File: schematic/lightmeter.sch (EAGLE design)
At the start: 67 parts, among them Q1 NCHANNELMOSFET, Q2 NCHANNELMOSFET, Q3 PCHANNELMOSFET

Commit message: More work on pcb layout.
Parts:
- renumbered R100 to R2, R1300 to R13, R1400 to R14, R200 to R1, R600 to R6, R800 to R8
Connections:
- removed net N$2: D2.A
- net VUSB: now also D2.A
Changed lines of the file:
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@@
 <part name="R700" library="resistor" deviceset="R-EU_" device="R0402" value="10k"/>
 <part name="GND8" library="supply1" deviceset="GND" device=""/>
-<part name="R800" library="resistor" deviceset="R-EU_" device="R0402" value="390k"/>
+<part name="R8" library="resistor" deviceset="R-EU_" device="R0402" value="390k"/>
 <part name="C15" library="rcl" deviceset="C-EU" device="C0402" value="1u"/>
 <part name="C16" library="rcl" deviceset="C-EU" device="C0402" value="1u"/>
@@
 <part name="GND28" library="supply1" deviceset="GND" device=""/>
 <part name="GND31" library="supply1" deviceset="GND" device=""/>
-<part name="R100" library="resistor" deviceset="R-EU_" device="R0402" value="15k"/>
-<part name="R200" library="resistor" deviceset="R-EU_" device="R0402" value="15k"/>
+<part name="R2" library="resistor" deviceset="R-EU_" device="R0402" value="15k"/>
+<part name="R1" library="resistor" deviceset="R-EU_" device="R0402" value="15k"/>
 <part name="GND9" library="supply1" deviceset="GND" device=""/>
 <part name="GND33" library="supply1" deviceset="GND" device=""/>
@@
 <part name="C24" library="rcl" deviceset="C-EU" device="C0402" value="1u"/>
 <part name="U$3" library="lightmeter" deviceset="LIBAT" device=""/>
-<part name="R1300" library="resistor" deviceset="R-EU_" device="R0402" value="500k"/>
-<part name="R1400" library="resistor" deviceset="R-EU_" device="R0402" value="500k"/>
+<part name="R13" library="resistor" deviceset="R-EU_" device="R0402" value="500k"/>
+<part name="R14" library="resistor" deviceset="R-EU_" device="R0402" value="500k"/>
 <part name="GND7" library="supply1" deviceset="GND" device=""/>
 <part name="P+4" library="supply1" deviceset="VCC" device=""/>
@@
 <part name="D3" library="lightmeter" deviceset="GSOT04-E3-08" device=""/>
 <part name="GND32" library="supply1" deviceset="GND" device=""/>
-<part name="R600" library="resistor" deviceset="R-EU_" device="R0402" value="10k"/>
+<part name="R6" library="resistor" deviceset="R-EU_" device="R0402" value="10k"/>
 <part name="IC$7" library="lightmeter" deviceset="NOA1212" device=""/>
 <part name="IC$8" library="lightmeter" deviceset="NOA1212" device=""/>
@@
 <instance part="R700" gate="G$1" x="160.02" y="0"/>
 <instance part="GND8" gate="1" x="-55.118" y="-108.458" rot="R270"/>
-<instance part="R800" gate="G$1" x="177.8" y="-10.16"/>
+<instance part="R8" gate="G$1" x="177.8" y="-10.16"/>
 <instance part="C15" gate="G$1" x="193.04" y="50.8" rot="R90"/>
 <instance part="C16" gate="G$1" x="177.8" y="48.26" rot="R90"/>
@@
 <instance part="GND28" gate="1" x="11.684" y="-118.618" rot="R90"/>
 <instance part="GND31" gate="1" x="-99.06" y="93.98" rot="R270"/>
-<instance part="R100" gate="G$1" x="-111.76" y="88.9"/>
-<instance part="R200" gate="G$1" x="-113.538" y="86.36"/>
+<instance part="R2" gate="G$1" x="-111.76" y="88.9"/>
+<instance part="R1" gate="G$1" x="-113.538" y="86.36"/>
 <instance part="GND9" gate="1" x="-117.856" y="98.298" rot="R180"/>
 <instance part="GND33" gate="1" x="-118.618" y="78.74"/>
@@
 <instance part="C24" gate="G$1" x="-76.2" y="-78.74"/>
 <instance part="U$3" gate="G$1" x="-132.08" y="-12.7"/>
-<instance part="R1300" gate="G$1" x="-111.76" y="-124.46"/>
-<instance part="R1400" gate="G$1" x="-91.44" y="-124.46"/>
+<instance part="R13" gate="G$1" x="-111.76" y="-124.46"/>
+<instance part="R14" gate="G$1" x="-91.44" y="-124.46"/>
 <instance part="GND7" gate="1" x="-81.788" y="-124.46" rot="R90"/>
 <instance part="P+4" gate="VCC" x="-124.46" y="-124.46" rot="R90"/>
@@
 <instance part="D3" gate="G$1" x="96.52" y="40.64" rot="R90"/>
 <instance part="GND32" gate="1" x="96.52" y="20.32"/>
-<instance part="R600" gate="G$1" x="96.52" y="30.48" rot="R90"/>
+<instance part="R6" gate="G$1" x="96.52" y="30.48" rot="R90"/>
 <instance part="IC$7" gate="G$1" x="167.64" y="-60.96"/>
 <instance part="IC$8" gate="G$1" x="167.64" y="-86.36"/>
@@
 <wire x1="152.4" y1="-17.78" x2="152.4" y2="-20.32" width="0.1524" layer="91"/>
 <pinref part="GND15" gate="1" pin="GND"/>
-<pinref part="R800" gate="G$1" pin="1"/>
+<pinref part="R8" gate="G$1" pin="1"/>
 <wire x1="172.72" y1="-10.16" x2="152.4" y2="-10.16" width="0.1524" layer="91"/>
 <wire x1="152.4" y1="-10.16" x2="152.4" y2="-17.78" width="0.1524" layer="91"/>
@@
 <wire x1="-118.618" y1="81.28" x2="-118.618" y2="86.36" width="0.1524" layer="91"/>
 <pinref part="GND33" gate="1" pin="GND"/>
-<pinref part="R200" gate="G$1" pin="1"/>
+<pinref part="R1" gate="G$1" pin="1"/>
 </segment>
 <segment>
@@
 <wire x1="-117.856" y1="88.9" x2="-117.856" y2="95.758" width="0.1524" layer="91"/>
 <pinref part="GND9" gate="1" pin="GND"/>
-<pinref part="R100" gate="G$1" pin="1"/>
+<pinref part="R2" gate="G$1" pin="1"/>
 </segment>
 <segment>
@@
 </segment>
 <segment>
-<pinref part="R1400" gate="G$1" pin="2"/>
+<pinref part="R14" gate="G$1" pin="2"/>
 <wire x1="-86.36" y1="-124.46" x2="-84.328" y2="-124.46" width="0.1524" layer="91"/>
 <pinref part="GND7" gate="1" pin="GND"/>
 </segment>
 <segment>
-<pinref part="R600" gate="G$1" pin="1"/>
+<pinref part="R6" gate="G$1" pin="1"/>
 <pinref part="GND32" gate="1" pin="GND"/>
 <wire x1="96.52" y1="25.4" x2="96.52" y2="22.86" width="0.1524" layer="91"/>
@@
 </segment>
 <segment>
-<pinref part="R1300" gate="G$1" pin="1"/>
+<pinref part="R13" gate="G$1" pin="1"/>
 <pinref part="P+4" gate="VCC" pin="VCC"/>
 <wire x1="-121.92" y1="-124.46" x2="-116.84" y2="-124.46" width="0.1524" layer="91"/>
@@
 <pinref part="IC$4" gate="G$1" pin="IREF"/>
 <wire x1="203.2" y1="-10.16" x2="182.88" y2="-10.16" width="0.1524" layer="91"/>
-<pinref part="R800" gate="G$1" pin="2"/>
+<pinref part="R8" gate="G$1" pin="2"/>
 </segment>
 </net>
@@
 <pinref part="U1" gate="G$1" pin="VBUS"/>
 <wire x1="-88.9" y1="83.82" x2="-96.52" y2="83.82" width="0.1524" layer="91"/>
+</segment>
+<segment>
+<wire x1="-137.16" y1="-48.26" x2="-139.7" y2="-48.26" width="0.1524" layer="91"/>
+<wire x1="-137.16" y1="-48.26" x2="-137.16" y2="-38.1" width="0.1524" layer="91"/>
+<pinref part="D2" gate="G$1" pin="A"/>
+<wire x1="-132.08" y1="-38.1" x2="-137.16" y2="-38.1" width="0.1524" layer="91"/>
+<label x="-139.7" y="-48.26" size="1.778" layer="95" rot="R180" xref="yes"/>
 </segment>
 </net>
@@
 <segment>
 <wire x1="-88.9" y1="88.9" x2="-101.6" y2="88.9" width="0.1524" layer="91"/>
-<pinref part="R100" gate="G$1" pin="2"/>
+<pinref part="R2" gate="G$1" pin="2"/>
 <pinref part="U1" gate="G$1" pin="D+"/>
 <wire x1="-101.6" y1="88.9" x2="-106.68" y2="88.9" width="0.1524" layer="91"/>
@@
 <net name="BATVOLTAGE" class="0">
 <segment>
-<pinref part="R1300" gate="G$1" pin="2"/>
-<pinref part="R1400" gate="G$1" pin="1"/>
+<pinref part="R13" gate="G$1" pin="2"/>
+<pinref part="R14" gate="G$1" pin="1"/>
 <wire x1="-106.68" y1="-124.46" x2="-96.52" y2="-124.46" width="0.1524" layer="91"/>
 <label x="-101.6" y="-124.46" size="1.778" layer="95" rot="R90" xref="yes"/>
@@
 <net name="N$13" class="0">
 <segment>
-<pinref part="R600" gate="G$1" pin="2"/>
+<pinref part="R6" gate="G$1" pin="2"/>
 <pinref part="D3" gate="G$1" pin="A"/>
 <wire x1="96.52" y1="35.56" x2="96.52" y2="38.1" width="0.1524" layer="91"/>
@@
 <segment>
 <wire x1="-88.9" y1="86.36" x2="-99.06" y2="86.36" width="0.1524" layer="91"/>
-<pinref part="R200" gate="G$1" pin="2"/>
+<pinref part="R1" gate="G$1" pin="2"/>
 <pinref part="U1" gate="G$1" pin="D-"/>
 <wire x1="-99.06" y1="86.36" x2="-108.458" y2="86.36" width="0.1524" layer="91"/>
@@
 </segment>
 </net>
-<net name="N$2" class="0">
-<segment>
-<wire x1="-137.16" y1="-48.26" x2="-139.7" y2="-48.26" width="0.1524" layer="91"/>
-<wire x1="-137.16" y1="-48.26" x2="-137.16" y2="-38.1" width="0.1524" layer="91"/>
-<pinref part="D2" gate="G$1" pin="A"/>
-<wire x1="-132.08" y1="-38.1" x2="-137.16" y2="-38.1" width="0.1524" layer="91"/>
-<label x="-139.7" y="-48.26" size="1.778" layer="95" rot="R180" xref="yes"/>
-</segment>
-</net>

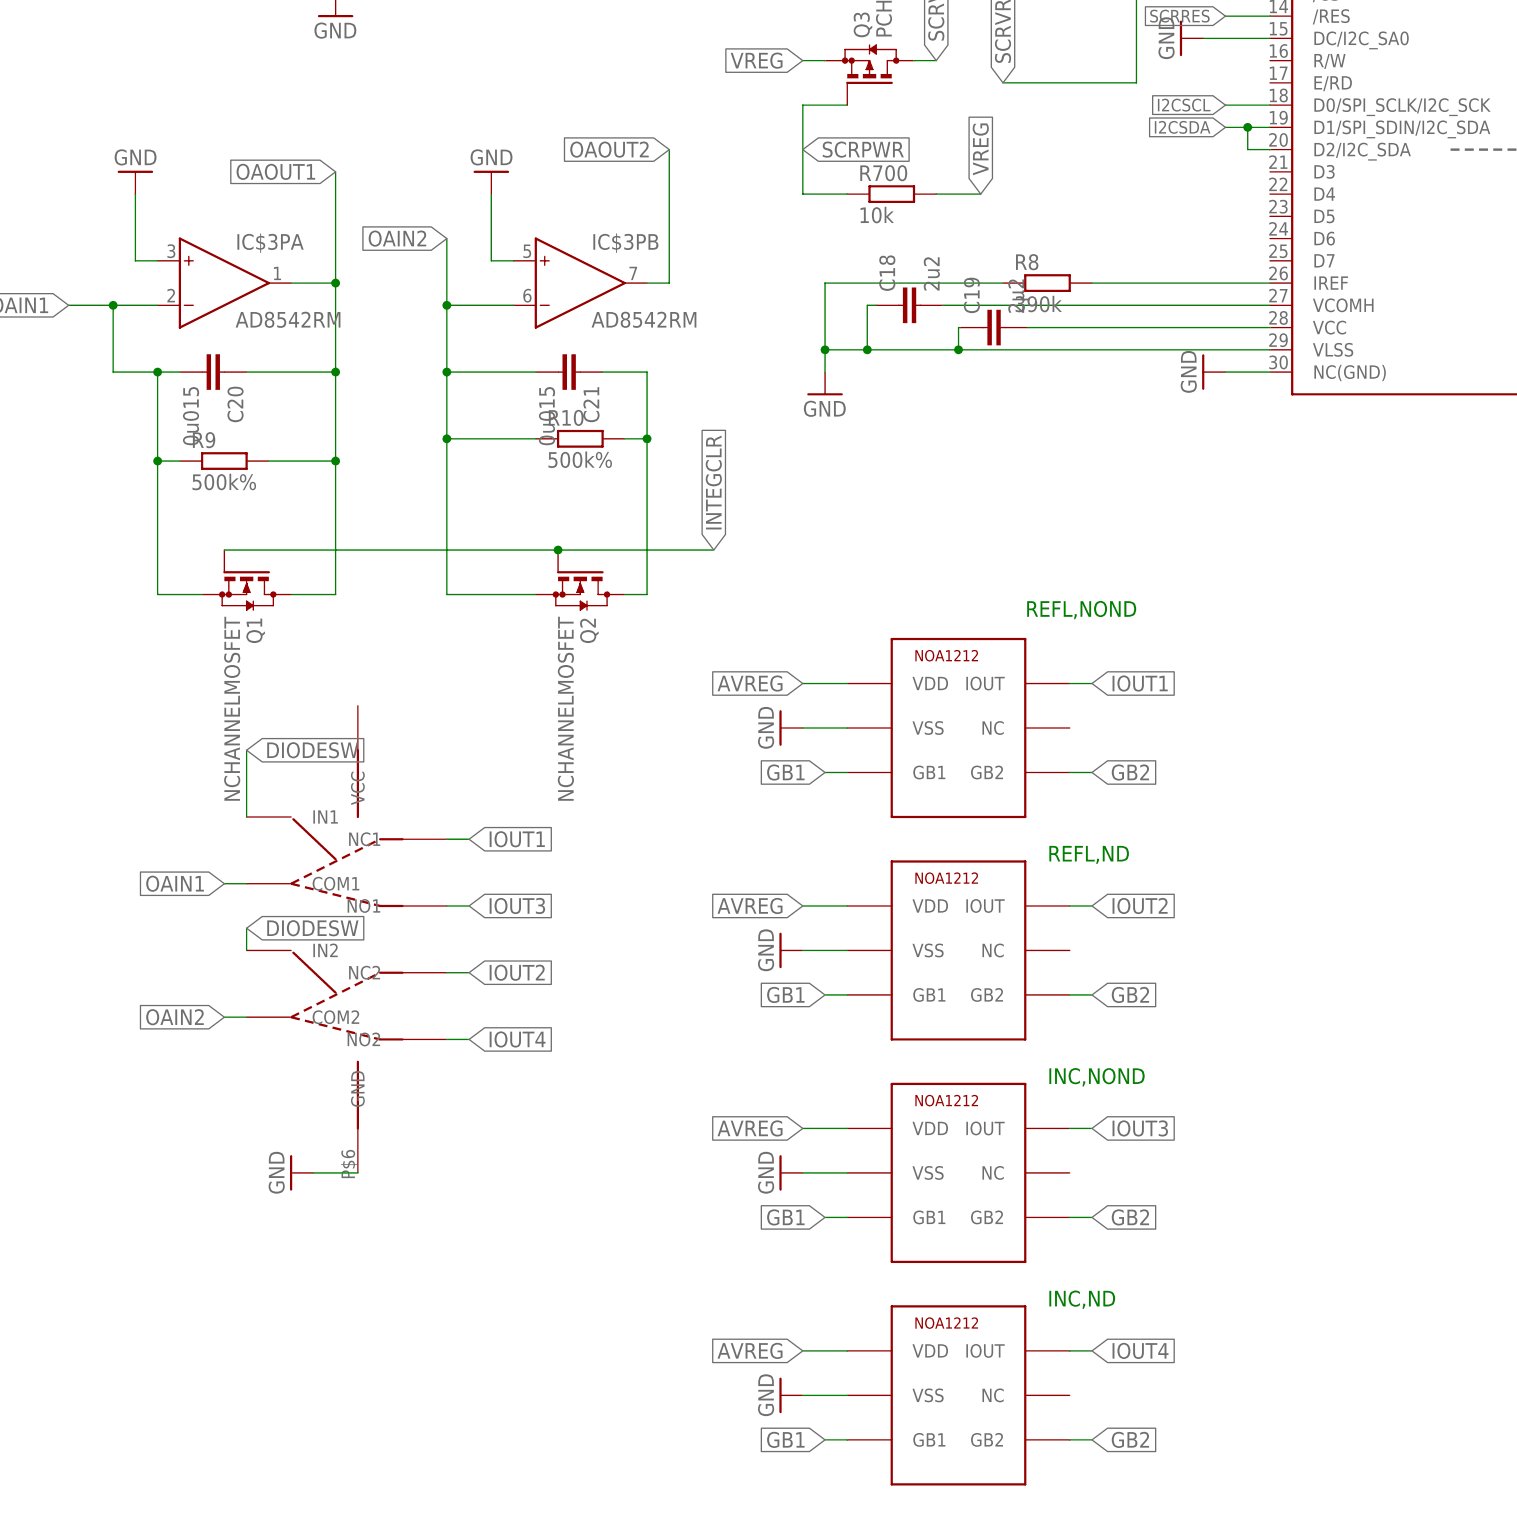
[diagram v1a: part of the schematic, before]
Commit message: More work on board layout.
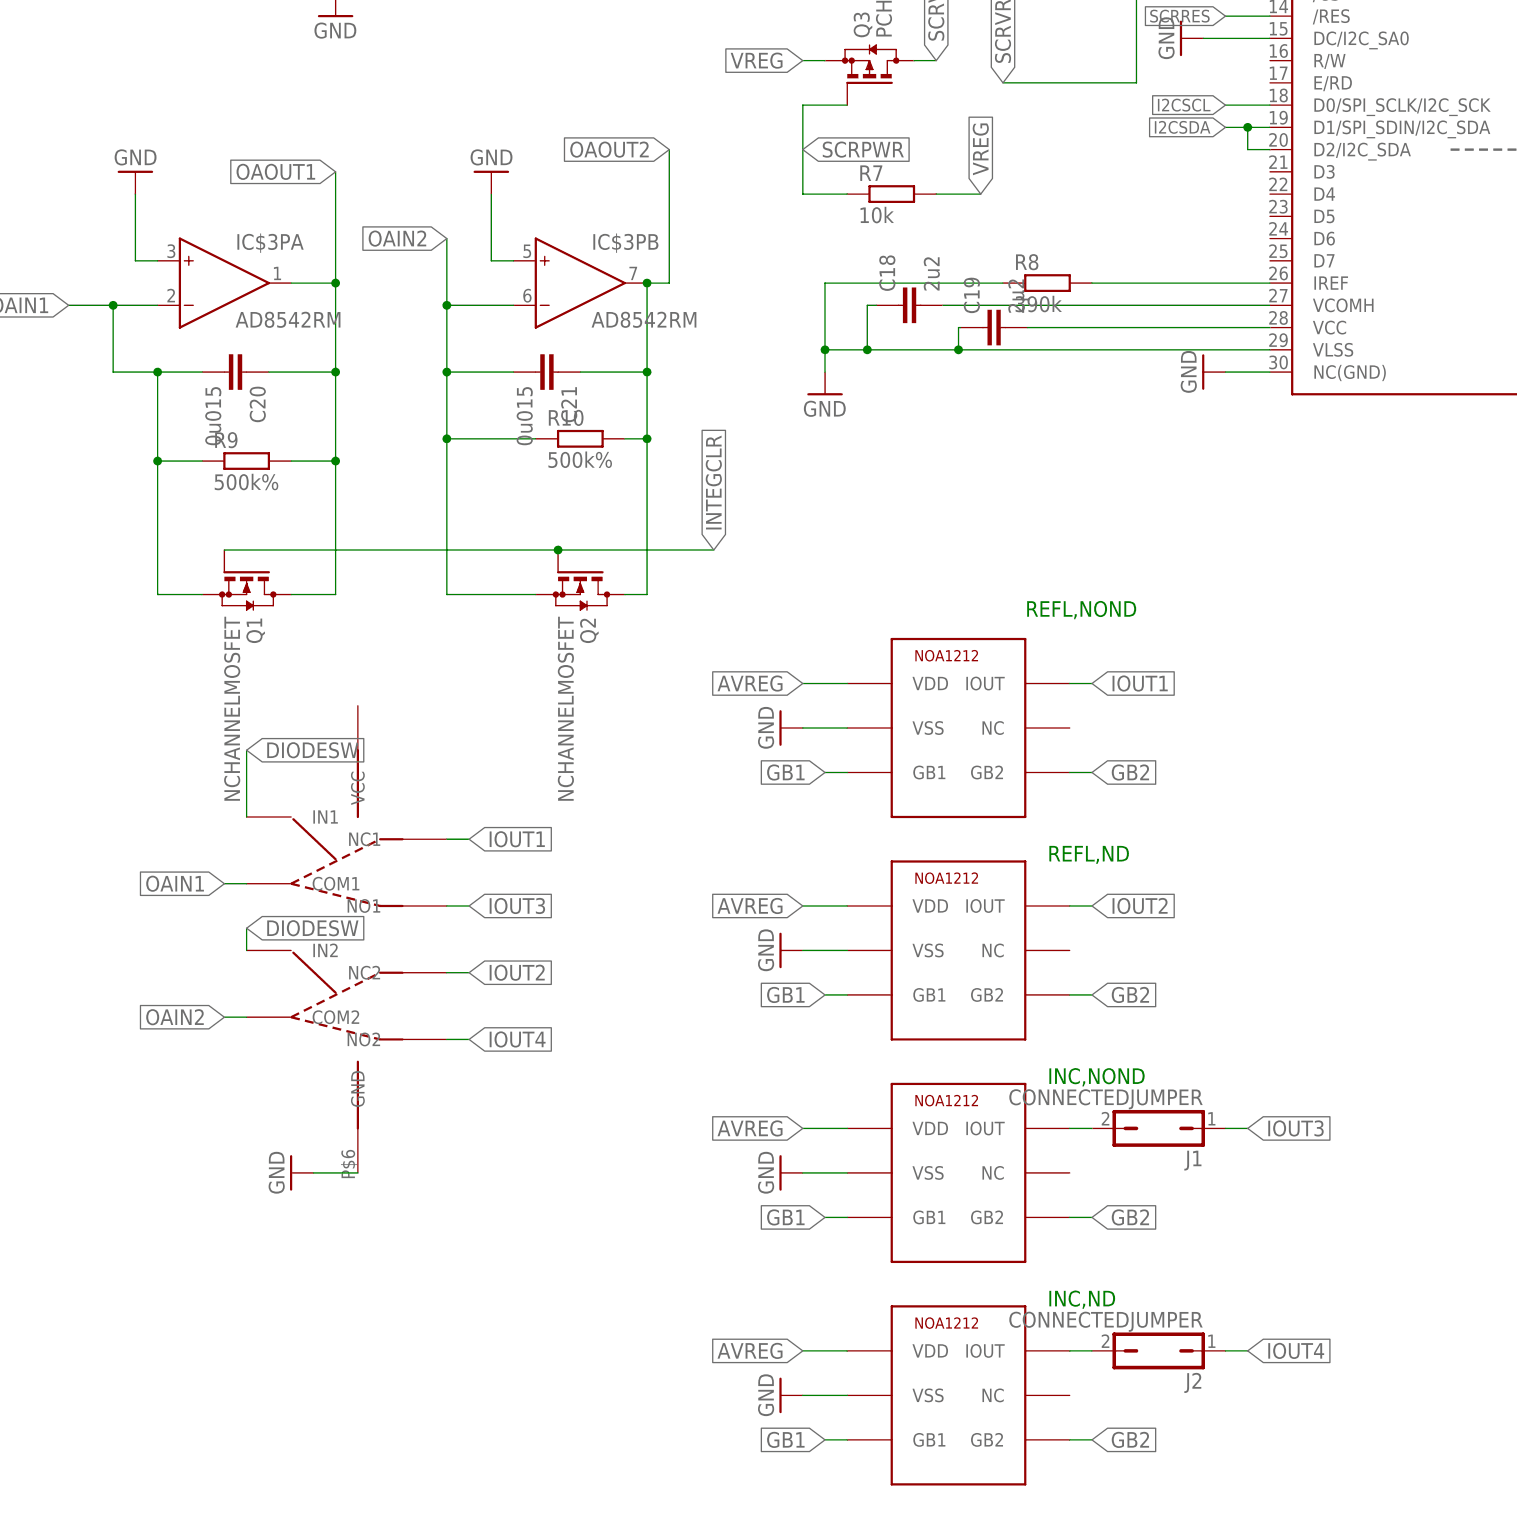
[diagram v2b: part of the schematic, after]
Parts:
- added J1, J2: CONNECTEDJUMPER, lightmeter:CONNECTEDJUMPER
- renumbered R700 to R7
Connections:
- removed net N$9: C21.1, Q2.D, R10.2
- new net N$1: IC$9.IOUT, J1.2
- new net N$2: IC$10.IOUT, J2.2
- net IOUT3: now also J1.1; no longer IC$9.IOUT
- net IOUT4: now also J2.1; no longer IC$10.IOUT
- net OAOUT2: now also C21.1, Q2.D, R10.2
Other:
- moved on the sheet: C20, C21, R9

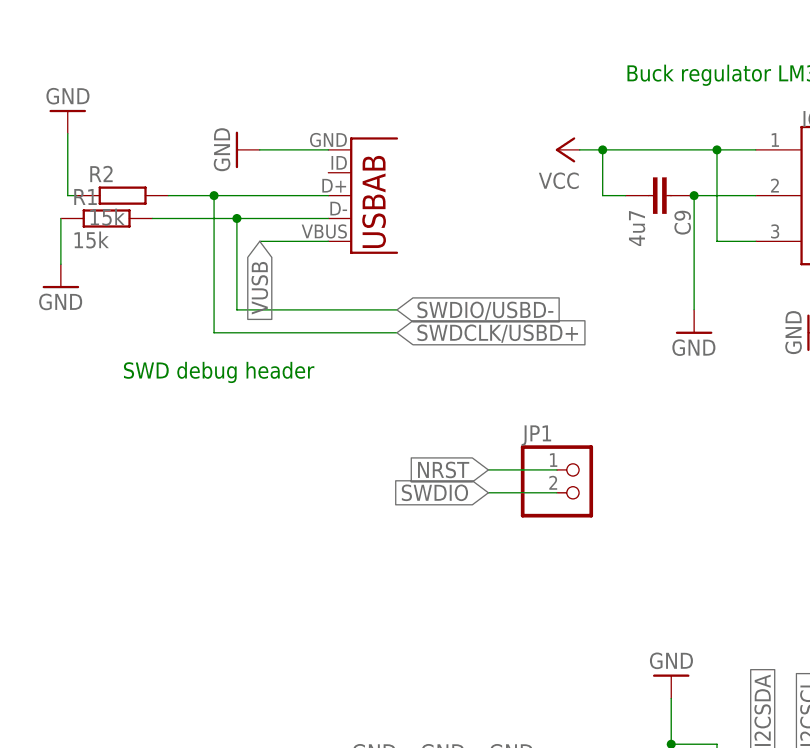
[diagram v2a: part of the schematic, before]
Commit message: Connect NRST to usb id pin so that only one pin header is (maybe) needed for swdio
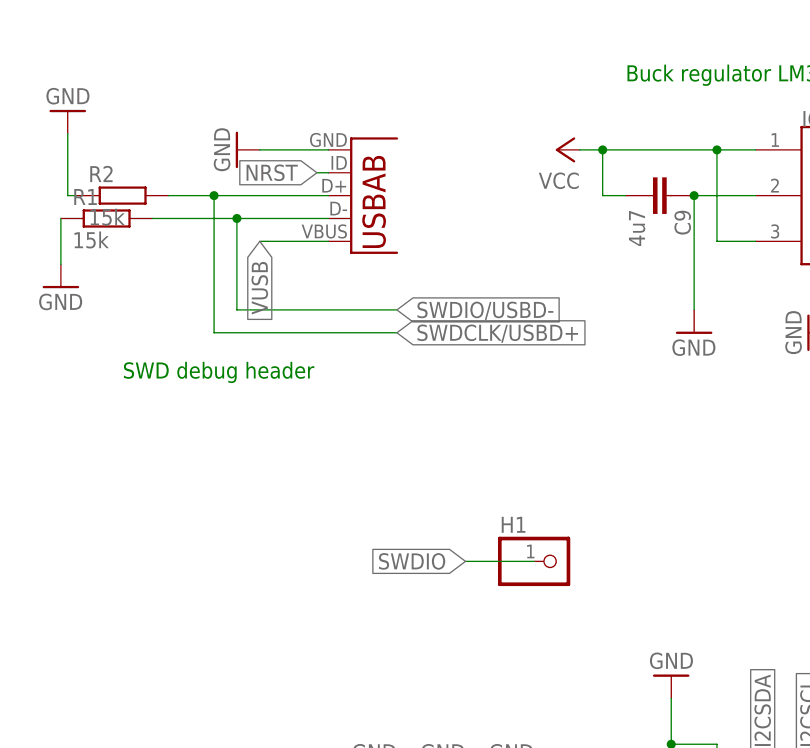
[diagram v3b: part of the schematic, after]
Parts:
- removed JP1: (no value), pinhead:PINHD-1X2
- added H1: (no value), pinhead:PINHD-1X1
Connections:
- net NRST: now also U1.USBID; no longer JP1.1
- net SWDIO: now also H1.1; no longer JP1.2
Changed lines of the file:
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@@
 <part name="S$2" library="lightmeter" deviceset="PTS540" device=""/>
 <part name="S$3" library="lightmeter" deviceset="PTS540" device=""/>
-<part name="JP1" library="pinhead" deviceset="PINHD-1X2" device=""/>
 <part name="D1" library="lightmeter" deviceset="SCHOTTKY-DIODE" device=""/>
 <part name="D2" library="lightmeter" deviceset="SCHOTTKY-DIODE" device=""/>
@@
 <part name="J1" library="lightmeter" deviceset="CONNECTEDJUMPER" device=""/>
 <part name="J2" library="lightmeter" deviceset="CONNECTEDJUMPER" device=""/>
+<part name="H1" library="pinhead" deviceset="PINHD-1X1" device=""/>
 </parts>
 <sheets>
@@
 <instance part="S$2" gate="G$1" x="-6.858" y="-95.504" rot="R270"/>
 <instance part="S$3" gate="G$1" x="8.382" y="-95.504" rot="R270"/>
-<instance part="JP1" gate="G$1" x="-60.96" y="55.88"/>
 <instance part="D1" gate="G$1" x="-129.54" y="-33.02"/>
 <instance part="D2" gate="G$1" x="-129.54" y="-38.1"/>
@@
 <instance part="J1" gate="G$1" x="190.5" y="-106.68"/>
 <instance part="J2" gate="G$1" x="190.5" y="-132.08"/>
+<instance part="H1" gate="G$1" x="-63.5" y="48.26"/>
 </instances>
 <busses>
@@
 </segment>
 <segment>
-<pinref part="JP1" gate="G$1" pin="1"/>
-<wire x1="-63.5" y1="58.42" x2="-71.12" y2="58.42" width="0.1524" layer="91"/>
-<label x="-71.12" y="58.42" size="1.778" layer="95" rot="R180" xref="yes"/>
+<pinref part="U1" gate="G$1" pin="USBID"/>
+<wire x1="-88.9" y1="91.44" x2="-90.17" y2="91.44" width="0.1524" layer="91"/>
+<label x="-90.17" y="91.44" size="1.778" layer="95" rot="R180" xref="yes"/>
 </segment>
 </net>
 <net name="SWDIO" class="0">
 <segment>
-<pinref part="JP1" gate="G$1" pin="2"/>
-<wire x1="-63.5" y1="55.88" x2="-71.12" y2="55.88" width="0.1524" layer="91"/>
-<label x="-71.12" y="55.88" size="1.778" layer="95" rot="R180" xref="yes"/>
-</segment>
-</net>
+<pinref part="H1" gate="G$1" pin="1"/>
+<wire x1="-66.04" y1="48.26" x2="-73.66" y2="48.26" width="0.1524" layer="91"/>
+<label x="-73.66" y="48.26" size="1.778" layer="95" rot="R180" xref="yes"/>
+</segment>
+</net>
